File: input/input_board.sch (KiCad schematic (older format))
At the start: 21 parts, among them J2 SCKB, J4 SCKA, J5 MCLK, J6 SDOB1, U1 DS90LV048, U2 FIN1047, U5 74LVC541A

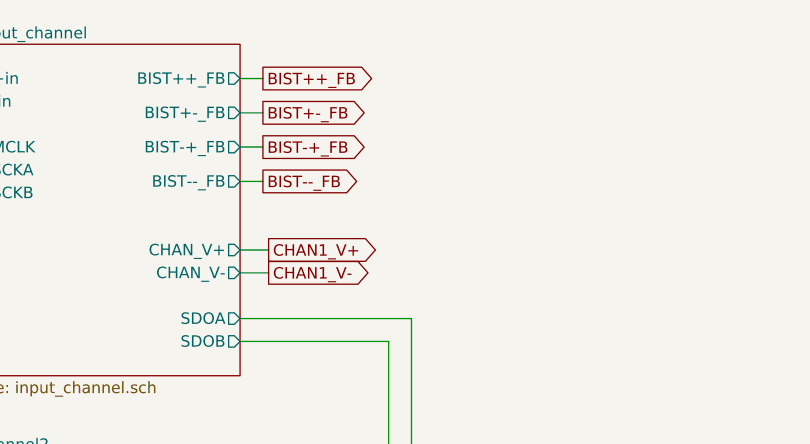
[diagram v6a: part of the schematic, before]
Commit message: notebook.txt and tweaks to comments in input board (no circuit changes).
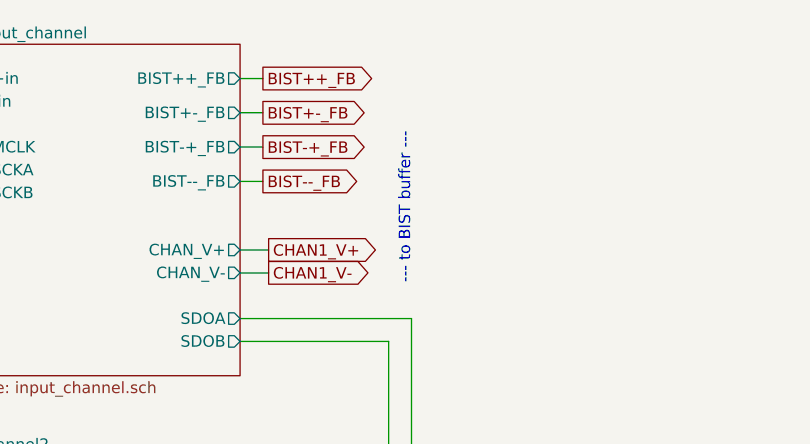
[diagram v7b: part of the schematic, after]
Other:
- note added: "--- to BIST buffer ---"
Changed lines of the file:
@@
 Wire Wire Line
 	8550 1000 8450 1000
+Text Notes 9200 1900 1    50   ~ 0
+--- to BIST buffer ---
 $EndSCHEMATC

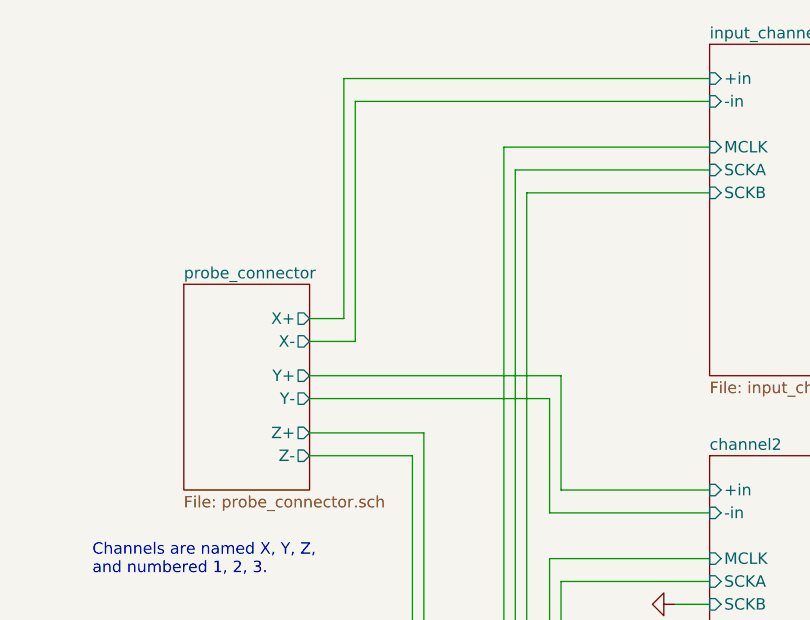
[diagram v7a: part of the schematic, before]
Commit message: Start of in_panel design, for input connectors on front panel, with RFI/ESD protection.  These components moved from input_board.
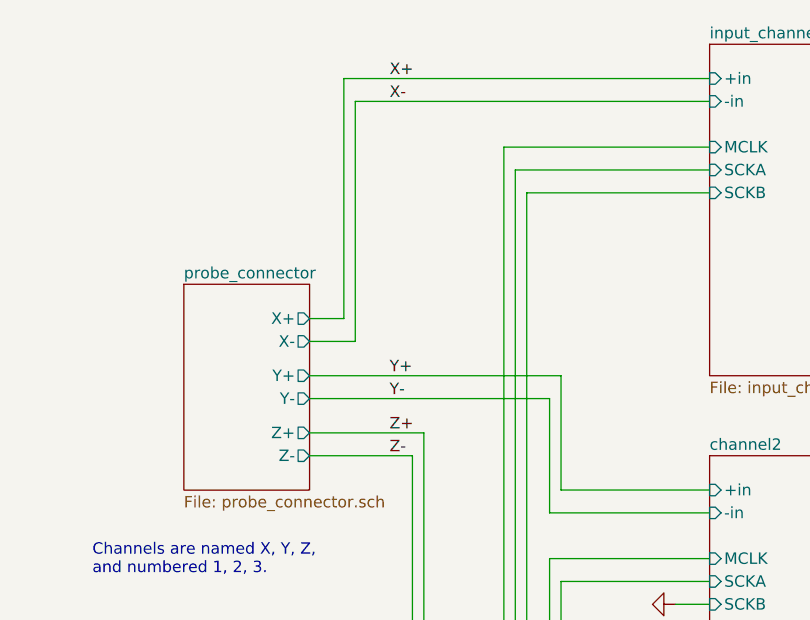
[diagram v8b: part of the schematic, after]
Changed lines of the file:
@@
 Text Notes 9200 1900 1    50   ~ 0
 --- to BIST buffer ---
+Text Label 5900 1000 0    50   ~ 0
+X+
+Text Label 5900 1100 0    50   ~ 0
+X-
+Text Label 5900 2300 0    50   ~ 0
+Y+
+Text Label 5900 2400 0    50   ~ 0
+Y-
+Text Label 5900 2550 0    50   ~ 0
+Z+
+Text Label 5900 2650 0    50   ~ 0
+Z-
 $EndSCHEMATC
